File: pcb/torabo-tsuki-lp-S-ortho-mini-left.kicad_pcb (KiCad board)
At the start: 2 copper layers, 138.8 x 69 mm, 72 parts, among them J101 Conn_01x06_MountingPin, SW10 SW_Push, SW101 SW_SPDT, SW11 SW_Push, SW12 SW_Push, SW13 SW_Push, SW15 SW_Push, SW16 SW_Push, SW17 SW_Push, SW18 SW_Push, SW19 SW_Push, SW20 SW_Push, SW22 SW_Push, SW23 SW_Push, SW24 SW_Push, SW25 SW_Push, SW26 SW_Push, SW27 SW_Push, SW28 SW_Push, SW29 SW_Push, SW30 SW_Push, SW31 SW_Push, SW32 SW_Push, SW33 SW_Push, SW34 SW_Push, SW35 SW_Push, SW8 SW_Push, SW9 SW_Push, U101 XIAO nRF52840 Plus, U102 XCL103D333CR-G, U103 XC8111AA01MR-G

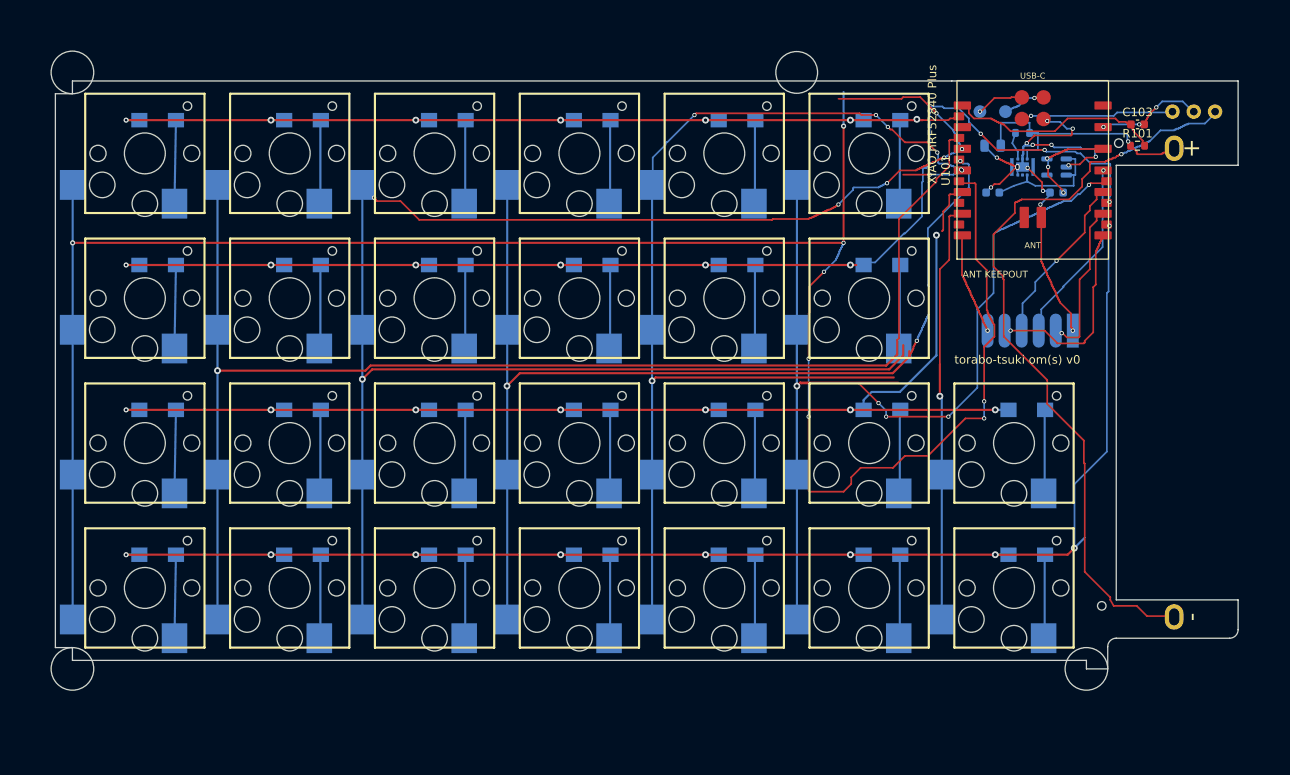
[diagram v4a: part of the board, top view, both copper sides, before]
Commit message: Convert split PCBs to column stagger
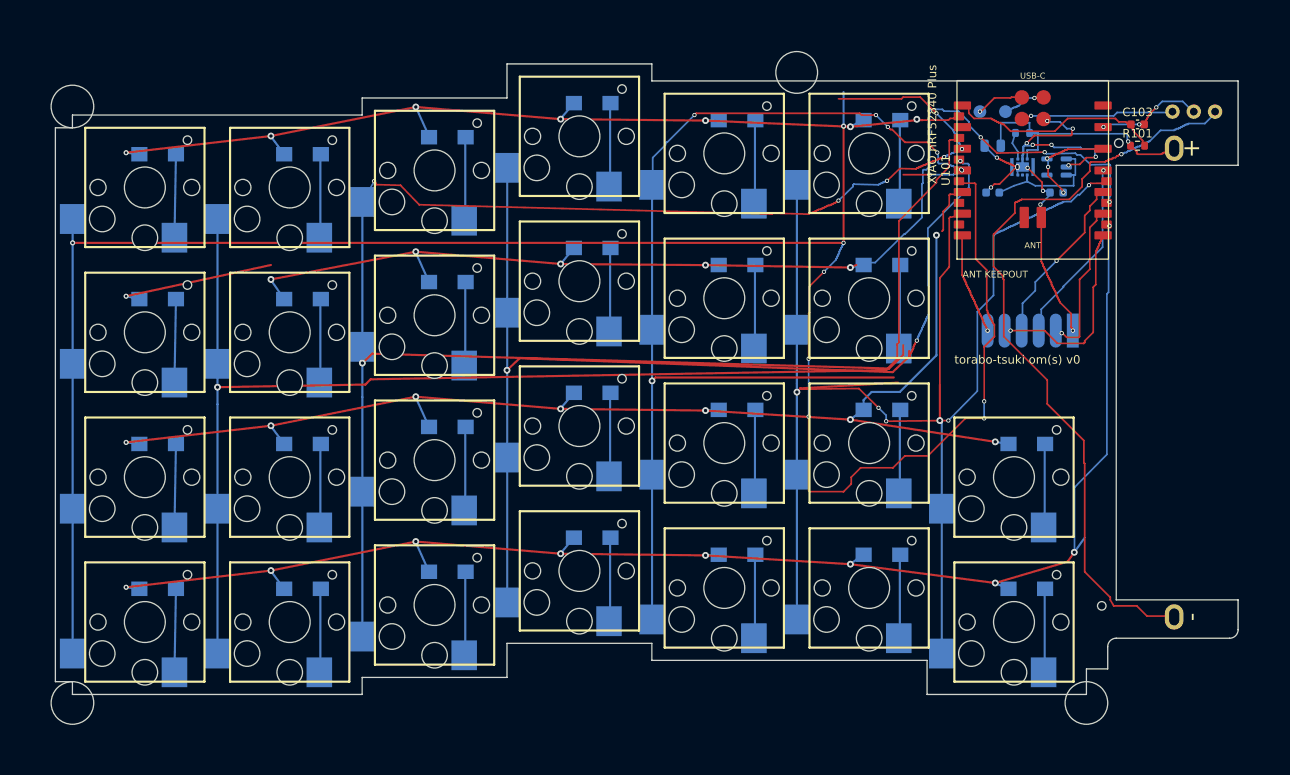
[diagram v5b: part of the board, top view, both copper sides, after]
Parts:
- moved D15 4.00 mm to (20.5, 68.1)
- moved D16 4.00 mm to (37.5, 68.1)
- moved D22 4.00 mm to (20.5, 85.1)
- moved D23 4.00 mm to (37.5, 85.1)
- moved D28 4.00 mm to (122.5, 85.1)
- moved D29 4.00 mm to (20.5, 102.1)
- moved D30 4.00 mm to (37.5, 102.1)
- moved D35 4.00 mm to (122.5, 102.1)
- moved D8 4.00 mm to (20.5, 51.1)
- moved D9 4.00 mm to (37.5, 51.1)
- moved REF** 4.00 mm to (10.5, 45.5)
- moved REF** 4.00 mm to (129.5, 115.5)
- moved REF** 4.00 mm to (10.5, 115.5)
- moved SW15 4.00 mm to (19.0, 72.0)
- moved SW16 4.00 mm to (36.0, 72.0)
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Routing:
- net /left/ROW4: track 164.1 -> 171.1 mm
- net /left/ROW3: track 145.2 -> 150.7 mm
- net /left/ROW1: track 108.0 -> 113.1 mm
- net /left/ROW2: track 146.8 -> 151.8 mm
- net /left/COL6: track 49.5 -> 53.3 mm
- net /left/COL2: track 210.6 -> 211.1 mm
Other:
- board size 138.8 x 69 mm -> 138.8 x 74 mm

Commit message: Refine staggered PCB outlines and mounting clearances
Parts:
- moved REF** 4.50 mm to (134.0, 115.5)
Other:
- outline, holes or cut-outs redrawn
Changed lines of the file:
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@@
 	(footprint "Library:MountingHole_5mm"
 		(layer "F.Cu")
-		(at 129.5 115.5)
+		(at 134 115.5)
 		(descr "Mounting Hole 5mm, no annular")
 		(tags "mounting hole 5mm no annular")
@@
 	)
 	(gr_line
-		(start 129.5 111.5)
-		(end 129.5 114.5)
-		(stroke
-			(width 0.1)
-			(type default)
-		)
-		(layer "Edge.Cuts")
-	)
-	(gr_line
-		(start 129.5 114.5)
+		(start 125.5 114.5)
 		(end 110.8 114.5)
 		(stroke
@@
 	)
 	(gr_line
-		(start 132 108.9)
-		(end 132 111.5)
-		(stroke
-			(width 0.1)
-			(type default)
-		)
-		(layer "Edge.Cuts")
-	)
-	(gr_arc
-		(start 132 108.9)
-		(mid 132.292893 108.192893)
-		(end 133 107.9)
-		(stroke
-			(width 0.1)
-			(type default)
-		)
-		(layer "Edge.Cuts")
-	)
-	(gr_line
-		(start 132 111.5)
-		(end 129.5 111.5)
-		(stroke
-			(width 0.1)
-			(type default)
-		)
-		(layer "Edge.Cuts")
-	)
-	(gr_line
 		(start 133 52.4)
 		(end 133 103.4)
@@
 	)
 	(gr_line
-		(start 146.3 107.9)
-		(end 133 107.9)
-		(stroke
-			(width 0.1)
-			(type default)
-		)
-		(layer "Edge.Cuts")
-	)
-	(gr_line
 		(start 147.3 42.5)
 		(end 147.3 52.4)
@@
 	(gr_line
 		(start 147.3 103.4)
-		(end 147.3 106.9)
+		(end 147.3 114.5)
 		(stroke
 			(width 0.1)
@@
 		(layer "Edge.Cuts")
 	)
-	(gr_arc
-		(start 147.3 106.9)
-		(mid 147.007107 107.607107)
-		(end 146.3 107.9)
+	(gr_line
+		(start 147.3 114.5)
+		(end 125.5 114.5)
 		(stroke
 			(width 0.1)
@@
 	)
 	(zone
-		(net "+BATT")
+		(net "/left/RESET_N")
 		(layer "F.Cu")
 		(hatch none 0.1)
-		(priority 30000)
+		(priority 30001)
 		(attr
 			(teardrop
@@
 		(polygon
 			(pts
-				(xy 141.9 47.9) (xy 141.9 47.7) (xy 140.719558 46.8) (xy 139.799 47.8) (xy 140.719558 48.8)
+				(xy 138.663541 44.917808) (xy 138.877915 45.046432) (xy 140.139234 44.157059) (xy 139.645885 43.523526)
+				(xy 138.754093 43.416685)
 			)
 		)
@@
 	)
 	(zone
-		(net "/left/RESET_N")
+		(net "/left/COL4")
 		(layer "F.Cu")
 		(hatch none 0.1)
-		(priority 30001)
+		(priority 30073)
 		(attr
 			(teardrop
@@
 		(polygon
 			(pts
-				(xy 138.663541 44.917808) (xy 138.877915 45.046432) (xy 140.139234 44.157059) (xy 139.645885 43.523526)
-				(xy 138.754093 43.416685)
+				(xy 79.155893 77.425) (xy 79.155893 77.175) (xy 78.925 77.175) (xy 78.836612 77.211612) (xy 78.47279 77.303422)
+				(xy 78.521873 77.703127) (xy 78.921578 77.75221) (xy 79.013388 77.388388)
 			)
 		)
 	)
 	(zone
-		(net "/left/COL4")
+		(net "+BATT")
 		(layer "F.Cu")
 		(hatch none 0.1)
-		(priority 30073)
+		(priority 30000)
 		(attr
 			(teardrop
@@
 		(polygon
 			(pts
-				(xy 79.155893 77.425) (xy 79.155893 77.175) (xy 78.925 77.175) (xy 78.836612 77.211612) (xy 78.47279 77.303422)
-				(xy 78.521873 77.703127) (xy 78.921578 77.75221) (xy 79.013388 77.388388)
+				(xy 141.9 47.9) (xy 141.9 47.7) (xy 140.719558 46.8) (xy 139.799 47.8) (xy 140.719558 48.8)
 			)
 		)
@@
 	)
 	(zone
-		(net "/left/COL4")
+		(net "Net-(D19-K)")
 		(layer "B.Cu")
 		(hatch none 0.1)
-		(priority 30052)
+		(priority 30073)
 		(attr
 			(teardrop
@@
 		(polygon
 			(pts
-				(xy 78.4 91.45) (xy 78.65 91.45) (xy 79.525 90.45) (xy 78.525 88.699) (xy 77.525 90.45)
+				(xy 90.475 65.8005) (xy 90.725 65.8005) (xy 91.45 64.9505) (xy 90.6 64.0995) (xy 89.75 64.9505)
 			)
 		)
 	)
 	(zone
-		(net "/left/COL4")
+		(net "Net-(D12-K)")
 		(layer "B.Cu")
 		(hatch none 0.1)
-		(priority 30051)
+		(priority 30077)
 		(attr
 			(teardrop
@@
 		(polygon
 			(pts
-				(xy 78.65 102.95) (xy 78.4 102.95) (xy 77.525 103.95) (xy 78.525 105.701) (xy 79.525 103.95)
+				(xy 90.475 48.8005) (xy 90.725 48.8005) (xy 91.45 47.9505) (xy 90.6 47.0995) (xy 89.75 47.9505)
 			)
 		)
 	)
 	(zone
-		(net "Net-(BT101--)")
+		(net "Net-(D12-K)")
 		(layer "B.Cu")
 		(hatch none 0.1)
-		(priority 30094)
+		(priority 30031)
 		(attr
 			(teardrop
@@
 		(polygon
 			(pts
-				(xy 144.7 41.804093) (xy 144.5 41.804093) (xy 143.850367 43.099313) (xy 144.6 43.505093) (xy 145.349633 43.099313)
+				(xy 90.725 54.15) (xy 90.475 54.15) (xy 89.6 55.15) (xy 90.6 56.901) (xy 91.6 55.15)
 			)
 		)
 	)
 	(zone
-		(net "Net-(D19-K)")
+		(net "/left/COL4")
 		(layer "B.Cu")
 		(hatch none 0.1)
-		(priority 30073)
+		(priority 30050)
 		(attr
 			(teardrop
@@
 		(polygon
 			(pts
-				(xy 90.475 65.8005) (xy 90.725 65.8005) (xy 91.45 64.9505) (xy 90.6 64.0995) (xy 89.75 64.9505)
+				(xy 78.65 85.95) (xy 78.4 85.95) (xy 77.525 86.95) (xy 78.525 88.701) (xy 79.525 86.95)
 			)
 		)
 	)
 	(zone
-		(net "Net-(D26-K)")
+		(net "Net-(BT101--)")
 		(layer "B.Cu")
 		(hatch none 0.1)
-		(priority 30087)
+		(priority 30067)
 		(attr
 			(teardrop
@@
 		(polygon
 			(pts
-				(xy 90.475 82.8005) (xy 90.725 82.8005) (xy 91.45 81.9505) (xy 90.6 81.0995) (xy 89.75 81.9505)
+				(xy 137.7 102.675) (xy 137.7 102.925) (xy 138.880442 103.8) (xy 139.801 102.8) (xy 138.880442 101.8)
 			)
 		)
 	)
 	(zone
-		(net "Net-(D12-K)")
+		(net "Net-(D26-K)")
 		(layer "B.Cu")
 		(hatch none 0.1)
-		(priority 30031)
+		(priority 30087)
 		(attr
 			(teardrop
@@
 		(polygon
 			(pts
-				(xy 90.725 54.15) (xy 90.475 54.15) (xy 89.6 55.15) (xy 90.6 56.901) (xy 91.6 55.15)
+				(xy 90.475 82.8005) (xy 90.725 82.8005) (xy 91.45 81.9505) (xy 90.6 81.0995) (xy 89.75 81.9505)
 			)
 		)
 	)
 	(zone
-		(net "Net-(D19-K)")
+		(net "/left/COL4")
 		(layer "B.Cu")
 		(hatch none 0.1)
-		(priority 30027)
+		(priority 30047)
 		(attr
 			(teardrop
@@
 		(polygon
 			(pts
-				(xy 90.725 71.15) (xy 90.475 71.15) (xy 89.6 72.15) (xy 90.6 73.901) (xy 91.6 72.15)
+				(xy 78.4 57.45) (xy 78.65 57.45) (xy 79.525 56.45) (xy 78.525 54.699) (xy 77.525 56.45)
 			)
 		)
 	)
 	(zone
-		(net "/left/COL4")
+		(net "Net-(D19-K)")
 		(layer "B.Cu")
 		(hatch none 0.1)
-		(priority 30050)
+		(priority 30027)
 		(attr
 			(teardrop
@@
 		(polygon
 			(pts
-				(xy 78.65 85.95) (xy 78.4 85.95) (xy 77.525 86.95) (xy 78.525 88.701) (xy 79.525 86.95)
+				(xy 90.725 71.15) (xy 90.475 71.15) (xy 89.6 72.15) (xy 90.6 73.901) (xy 91.6 72.15)
 			)
 		)
@@
 		(layer "B.Cu")
 		(hatch none 0.1)
-		(priority 30046)
+		(priority 30044)
 		(attr
 			(teardrop
@@
 		(polygon
 			(pts
-				(xy 78.65 68.95) (xy 78.4 68.95) (xy 77.525 69.95) (xy 78.525 71.701) (xy 79.525 69.95)
+				(xy 78.4 74.45) (xy 78.65 74.45) (xy 79.525 73.45) (xy 78.525 71.699) (xy 77.525 73.45)
 			)
 		)
 	)
 	(zone
-		(net "Net-(D12-K)")
+		(net "/left/COL4")
 		(layer "B.Cu")
 		(hatch none 0.1)
-		(priority 30077)
+		(priority 30156)
 		(attr
 			(teardrop
@@
 		(polygon
 			(pts
-				(xy 90.475 48.8005) (xy 90.725 48.8005) (xy 91.45 47.9505) (xy 90.6 47.0995) (xy 89.75 47.9505)
+				(xy 78.65 76.903422) (xy 78.4 76.903422) (xy 78.155448 77.546927) (xy 78.525 77.704422) (xy 78.894552 77.546927)
 			)
 		)
 	)
 	(zone
-		(net "/left/COL4")
+		(net "Net-(D33-K)")
 		(layer "B.Cu")
 		(hatch none 0.1)
-		(priority 30157)
+		(priority 30004)
 		(attr
 			(teardrop
@@
 		(polygon
 			(pts
-				(xy 78.4 78.496578) (xy 78.65 78.496578) (xy 78.894552 77.853073) (xy 78.525 77.695578) (xy 78.155448 77.853073)
+				(xy 90.725 105.15) (xy 90.475 105.15) (xy 89.6 106.15) (xy 90.6 107.901) (xy 91.6 106.15)
 			)
 		)
 	)
 	(zone
-		(net "Net-(D33-K)")
+		(net "/left/COL4")
 		(layer "B.Cu")
 		(hatch none 0.1)
-		(priority 30004)
+		(priority 30052)
 		(attr
 			(teardrop
@@
 		(polygon
 			(pts
-				(xy 90.725 105.15) (xy 90.475 105.15) (xy 89.6 106.15) (xy 90.6 107.901) (xy 91.6 106.15)
+				(xy 78.4 91.45) (xy 78.65 91.45) (xy 79.525 90.45) (xy 78.525 88.699) (xy 77.525 90.45)
 			)
 		)
 	)
 	(zone
-		(net "/left/COL4")
+		(net "Net-(D26-K)")
 		(layer "B.Cu")
 		(hatch none 0.1)
-		(priority 30044)
+		(priority 30006)
 		(attr
 			(teardrop
@@
 		(polygon
 			(pts
-				(xy 78.4 74.45) (xy 78.65 74.45) (xy 79.525 73.45) (xy 78.525 71.699) (xy 77.525 73.45)
+				(xy 90.725 88.15) (xy 90.475 88.15) (xy 89.6 89.15) (xy 90.6 90.901) (xy 91.6 89.15)
 			)
 		)
 	)
 	(zone
-		(net "Net-(BT101--)")
+		(net "/left/COL4")
 		(layer "B.Cu")
 		(hatch none 0.1)
-		(priority 30067)
+		(priority 30157)
 		(attr
 			(teardrop
@@
 		(polygon
 			(pts
-				(xy 137.7 102.675) (xy 137.7 102.925) (xy 138.880442 103.8) (xy 139.801 102.8) (xy 138.880442 101.8)
+				(xy 78.4 78.496578) (xy 78.65 78.496578) (xy 78.894552 77.853073) (xy 78.525 77.695578) (xy 78.155448 77.853073)
 			)
 		)
 	)
 	(zone
-		(net "/left/COL4")
+		(net "Net-(BT101--)")
 		(layer "B.Cu")
 		(hatch none 0.1)
-		(priority 30047)
+		(priority 30094)
 		(attr
 			(teardrop
@@
 		(polygon
 			(pts
-				(xy 78.4 57.45) (xy 78.65 57.45) (xy 79.525 56.45) (xy 78.525 54.699) (xy 77.525 56.45)
+				(xy 144.7 41.804093) (xy 144.5 41.804093) (xy 143.850367 43.099313) (xy 144.6 43.505093) (xy 145.349633 43.099313)
 			)
 		)
 	)
 	(zone
-		(net "Net-(D26-K)")
+		(net "/left/COL4")
 		(layer "B.Cu")
 		(hatch none 0.1)
-		(priority 30006)
+		(priority 30051)
 		(attr
 			(teardrop
@@
 		(polygon
 			(pts
-				(xy 90.725 88.15) (xy 90.475 88.15) (xy 89.6 89.15) (xy 90.6 90.901) (xy 91.6 89.15)
+				(xy 78.65 102.95) (xy 78.4 102.95) (xy 77.525 103.95) (xy 78.525 105.701) (xy 79.525 103.95)
 			)
 		)
@@
 		(layer "B.Cu")
 		(hatch none 0.1)
-		(priority 30156)
+		(priority 30046)
 		(attr
 			(teardrop
@@
 		(polygon
 			(pts
-				(xy 78.65 76.903422) (xy 78.4 76.903422) (xy 78.155448 77.546927) (xy 78.525 77.704422) (xy 78.894552 77.546927)
+				(xy 78.65 68.95) (xy 78.4 68.95) (xy 77.525 69.95) (xy 78.525 71.701) (xy 79.525 69.95)
 			)
 		)
